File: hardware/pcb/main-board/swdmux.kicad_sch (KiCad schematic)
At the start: 2 parts, among them U901 MUX

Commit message: make a start on RP2040 to replace the KB pico
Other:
- title: Z88R - Z88 Recreated -> Z88R - Z88 Recreation
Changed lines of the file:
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@@
 	(paper "A4")
 	(title_block
-		(title "Z88R - Z88 Recreated")
-		(date "2025-12-19")
-		(rev "20251219WIP")
+		(title "Z88R - Z88 Recreation")
+		(date "2025-12-30")
+		(rev "20251230WIP")
 		(company "Fountain and Menadue")
 	)

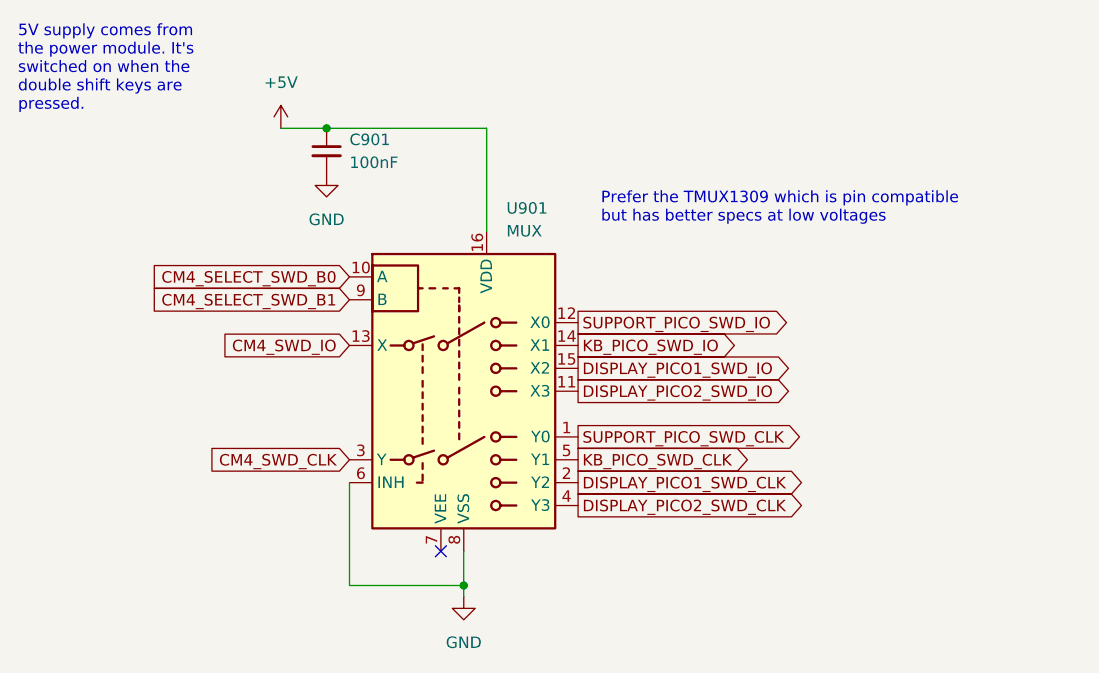
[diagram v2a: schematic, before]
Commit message: more work on KB pico replacement
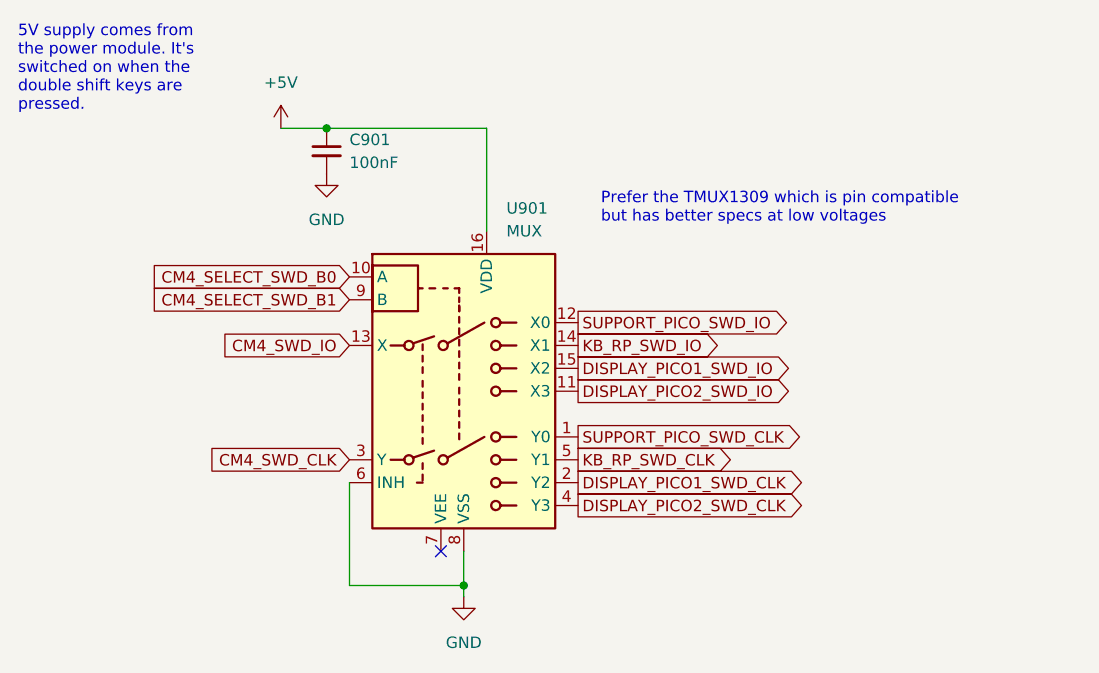
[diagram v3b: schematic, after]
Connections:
- net KB_PICO_SWD_CLK renamed KB_RP_SWD_CLK
- net KB_PICO_SWD_IO renamed KB_RP_SWD_IO
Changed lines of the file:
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@@
 		)
 	)
-	(global_label "KB_PICO_SWD_IO"
+	(global_label "KB_RP_SWD_IO"
 		(shape output)
 		(at 96.52 68.58 0)
@@
 		)
 		(property "Intersheetrefs" "${INTERSHEET_REFS}"
-			(at 114.6353 68.58 0)
+			(at 112.7 68.58 0)
 			(effects
 				(font
@@
 		)
 	)
-	(global_label "KB_PICO_SWD_CLK"
+	(global_label "KB_RP_SWD_CLK"
 		(shape output)
 		(at 96.52 81.28 0)
@@
 		)
 		(property "Intersheetrefs" "${INTERSHEET_REFS}"
-			(at 116.2681 81.28 0)
+			(at 114.3328 81.28 0)
 			(effects
 				(font

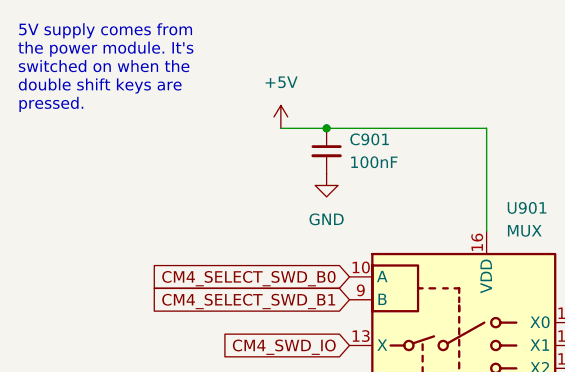
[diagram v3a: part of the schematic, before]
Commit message: more working out of the KB pico replacement
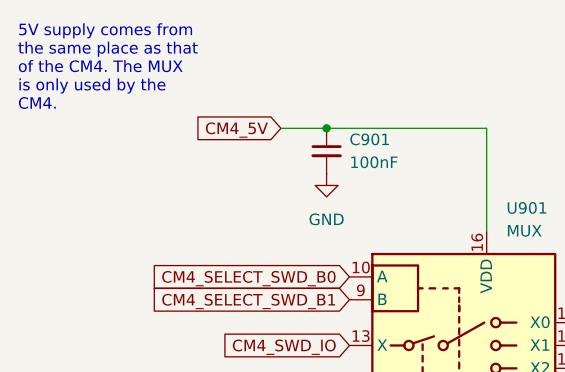
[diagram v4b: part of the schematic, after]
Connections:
- net +5V renamed CM4_5V
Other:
- note added: "5V supply comes from the same place as that of the CM4. The MUX is only used by the CM4."
- note removed: "5V supply comes from the power module. It's switched on when the double shift keys are pressed."
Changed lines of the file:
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@@
 		)
 	)
-	(text "5V supply comes from\nthe power module. It's\nswitched on when the\ndouble shift keys are\npressed."
+	(text "5V supply comes from\nthe same place as that\nof the CM4. The MUX \nis only used by the\nCM4."
 		(exclude_from_sim no)
 		(at 34.29 37.846 0)
@@
 				)
 				(justify left)
+				(hide yes)
+			)
+		)
+	)
+	(global_label "CM4_5V"
+		(shape input)
+		(at 63.5 44.45 180)
+		(fields_autoplaced yes)
+		(effects
+			(font
+				(size 1.27 1.27)
+			)
+			(justify right)
+		)
+		(property "Intersheetrefs" "${INTERSHEET_REFS}"
+			(at 53.9724 44.45 0)
+			(effects
+				(font
+					(size 1.27 1.27)
+				)
+				(justify right)
 				(hide yes)
 			)
@@
 					(unit 1)
 				)
-			)
-		)
-	)
-	(symbol
-		(lib_id "power:+5V")
-		(at 63.5 44.45 0)
-		(unit 1)
-		(exclude_from_sim no)
-		(in_bom yes)
-		(on_board yes)
-		(dnp no)
-		(fields_autoplaced yes)
-		(property "Reference" "#PWR0901"
-			(at 63.5 48.26 0)
-			(effects
-				(font
-					(size 1.27 1.27)
-				)
-				(hide yes)
-			)
-		)
-		(property "Value" "+5V"
-			(at 63.5 39.37 0)
-			(effects
-				(font
-					(size 1.27 1.27)
-				)
-			)
-		)
-		(property "Footprint" ""
-			(at 63.5 44.45 0)
-			(effects
-				(font
-					(size 1.27 1.27)
-				)
-				(hide yes)
-			)
-		)
-		(property "Datasheet" ""
-			(at 63.5 44.45 0)
-			(effects
-				(font
-					(size 1.27 1.27)
-				)
-				(hide yes)
-			)
-		)
-		(property "Description" "Power symbol creates a global label with name \"+5V\""
-			(at 63.5 44.45 0)
-			(effects
-				(font
-					(size 1.27 1.27)
-				)
-				(hide yes)
-			)
-		)
-		(pin "1"
-		)
-		(instances
-			(project ""
-				(path "/fdce8012-5f35-4f58-8abb-80214b4af8fe/a77ef2bd-e252-49fb-bafe-76bf661b7991"
-					(reference "#PWR0901")
-					(unit 1)
-				)

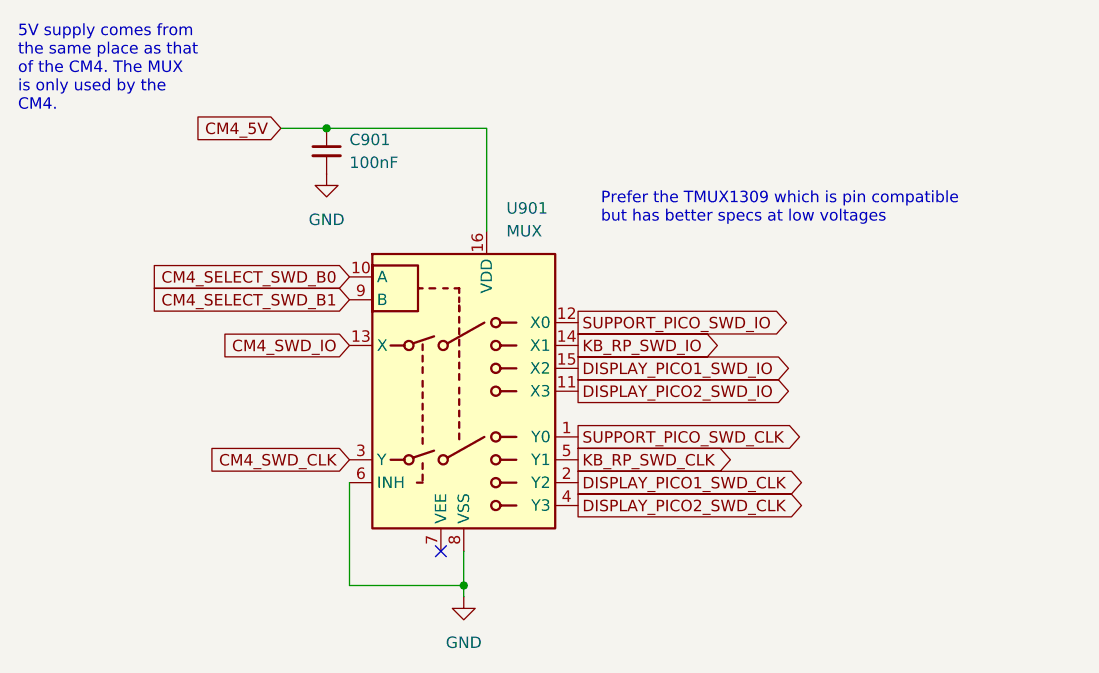
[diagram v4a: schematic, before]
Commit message: start the support pico rp2040 replacement
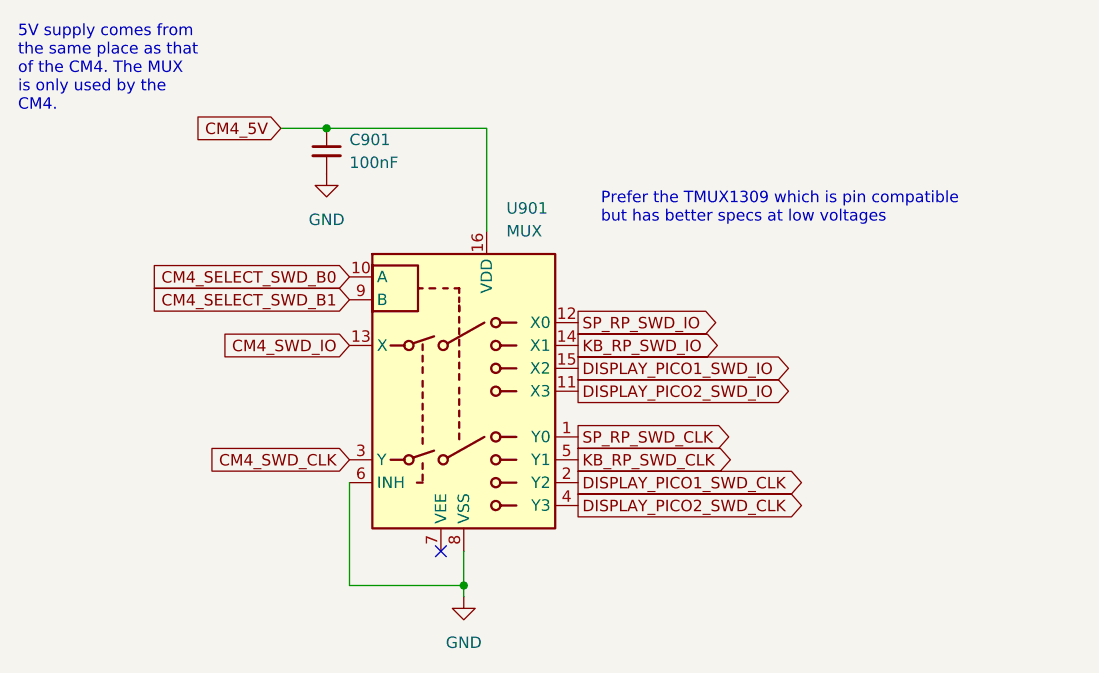
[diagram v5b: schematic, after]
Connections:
- net SUPPORT_PICO_SWD_CLK renamed SP_RP_SWD_CLK
- net SUPPORT_PICO_SWD_IO renamed SP_RP_SWD_IO
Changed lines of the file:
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@@
 	(title_block
 		(title "Z88R - Z88 Recreation")
-		(date "2025-12-30")
-		(rev "20251230WIP")
+		(date "2026-01-01")
+		(rev "20260101WIP")
 		(company "Fountain and Menadue")
 	)
@@
 		)
 	)
-	(global_label "SUPPORT_PICO_SWD_IO"
+	(global_label "SP_RP_SWD_IO"
 		(shape output)
 		(at 96.52 66.04 0)
@@
 		)
 		(property "Intersheetrefs" "${INTERSHEET_REFS}"
-			(at 120.7434 66.04 0)
+			(at 112.6395 66.04 0)
 			(effects
 				(font
@@
 		)
 	)
-	(global_label "SUPPORT_PICO_SWD_CLK"
+	(global_label "SP_RP_SWD_CLK"
 		(shape output)
 		(at 96.52 78.74 0)
@@
 		)
 		(property "Intersheetrefs" "${INTERSHEET_REFS}"
-			(at 122.3762 78.74 0)
-			(effects
-				(font
+			(at 114.2723 78.74 0)
+			(effects
+				(font

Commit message: tidy the keyboard comms
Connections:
- net DISPLAY_PICO1_SWD_CLK renamed APPB_PICO0_SWD_CLK
- net DISPLAY_PICO1_SWD_IO renamed APPB_PICO0_SWD_IO
- net DISPLAY_PICO2_SWD_CLK renamed APPB_PICO1_SWD_CLK
- net DISPLAY_PICO2_SWD_IO renamed APPB_PICO1_SWD_IO
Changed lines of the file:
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@@
 		)
 	)
-	(global_label "DISPLAY_PICO1_SWD_CLK"
+	(global_label "APPB_PICO0_SWD_CLK"
 		(shape output)
 		(at 96.52 83.82 0)
@@
 		)
 		(property "Intersheetrefs" "${INTERSHEET_REFS}"
-			(at 122.4972 83.82 0)
+			(at 119.8362 83.82 0)
 			(effects
 				(font
@@
 		)
 	)
-	(global_label "DISPLAY_PICO2_SWD_IO"
+	(global_label "APPB_PICO1_SWD_IO"
 		(shape output)
 		(at 96.52 73.66 0)
@@
 		)
 		(property "Intersheetrefs" "${INTERSHEET_REFS}"
-			(at 120.8644 73.66 0)
+			(at 118.2034 73.66 0)
 			(effects
 				(font
@@
 		)
 	)
-	(global_label "DISPLAY_PICO2_SWD_CLK"
+	(global_label "APPB_PICO1_SWD_CLK"
 		(shape output)
 		(at 96.52 86.36 0)
@@
 		)
 		(property "Intersheetrefs" "${INTERSHEET_REFS}"
-			(at 122.4972 86.36 0)
+			(at 119.8362 86.36 0)
 			(effects
 				(font
@@
 		)
 	)
-	(global_label "DISPLAY_PICO1_SWD_IO"
+	(global_label "APPB_PICO0_SWD_IO"
 		(shape output)
 		(at 96.52 71.12 0)
@@
 		)
 		(property "Intersheetrefs" "${INTERSHEET_REFS}"
-			(at 120.8644 71.12 0)
+			(at 118.2034 71.12 0)
 			(effects
 				(font

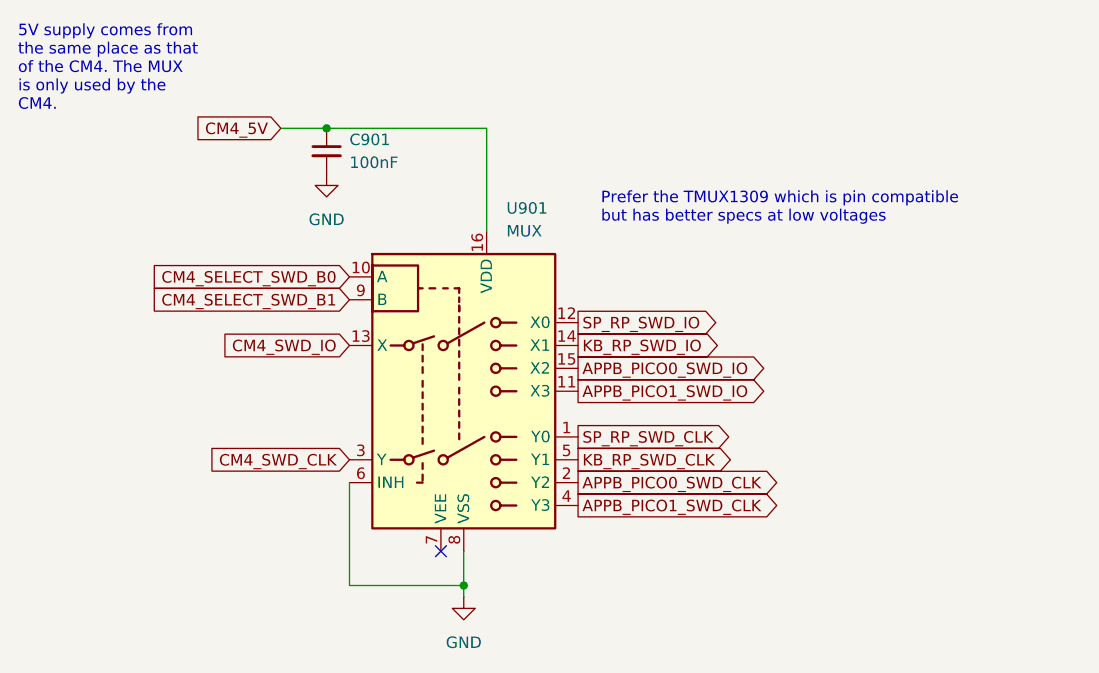
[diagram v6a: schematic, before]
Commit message: rename app board picos to 1 and 2, to match the application board schematics
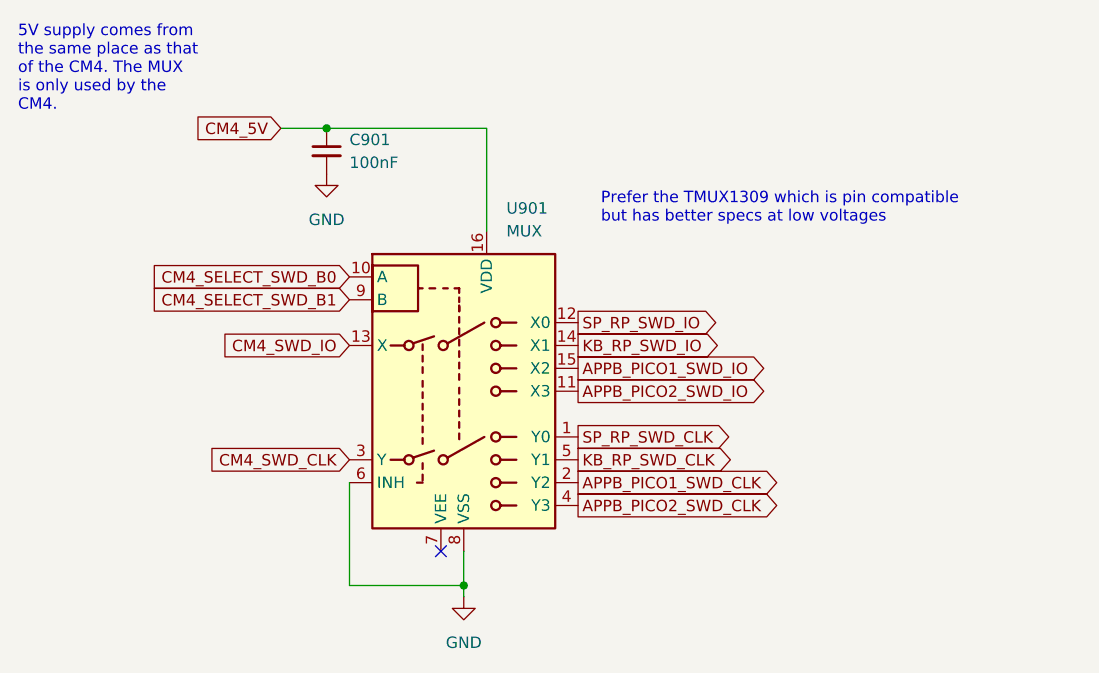
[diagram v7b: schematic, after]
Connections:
- net APPB_PICO0_SWD_CLK is gone; now on net APPB_PICO1_SWD_CLK: U901.2 (Y2)
- net APPB_PICO0_SWD_IO is gone; now on net APPB_PICO1_SWD_IO: U901.15 (X2)
- net APPB_PICO1_SWD_CLK: no longer U901.4 (Y3)
- net APPB_PICO1_SWD_IO: no longer U901.11 (X3)
- new net APPB_PICO2_SWD_CLK: U901.4 (Y3)
- new net APPB_PICO2_SWD_IO: U901.11 (X3)
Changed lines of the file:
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@@
 		)
 	)
-	(global_label "APPB_PICO0_SWD_CLK"
+	(global_label "APPB_PICO1_SWD_CLK"
 		(shape output)
 		(at 96.52 83.82 0)
@@
 		)
 	)
-	(global_label "APPB_PICO1_SWD_IO"
+	(global_label "APPB_PICO2_SWD_IO"
 		(shape output)
 		(at 96.52 73.66 0)
@@
 		)
 	)
-	(global_label "APPB_PICO1_SWD_CLK"
+	(global_label "APPB_PICO2_SWD_CLK"
 		(shape output)
 		(at 96.52 86.36 0)
@@
 		)
 	)
-	(global_label "APPB_PICO0_SWD_IO"
+	(global_label "APPB_PICO1_SWD_IO"
 		(shape output)
 		(at 96.52 71.12 0)
